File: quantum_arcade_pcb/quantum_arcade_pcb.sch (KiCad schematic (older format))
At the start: 429 parts, among them J20 J20, Q10 2N3904, Q11 2N3904, Q15 2N6044, Q16 2N6044, Q17 2N3904, Q7 2N3904, Q8 2N3906, Q9 2N3904, SW1 SW_DIP_x08, SW2 SW_DIP_x08, Y1 12.096MHz

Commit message: Finished 13 of 14 schematic pages
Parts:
- added A_5: LS157A, symbol quantum_arcade_pcb:LS157A
- added B_5, C_5: LS157B, symbol quantum_arcade_pcb:LS157B
- added B_6: AVG, symbol Star_Wars_Vector_PCB:AVG
- added C63: 220pf, symbol Device:C
- added unit 6 of F/H_4
- added F_8: LS175, symbol quantum_arcade_pcb:LS175
- added H_5: LS174, symbol quantum_arcade_pcb:LS174
- added H_6: S129, symbol Star_Wars_Vector_PCB:S129
- added H_7: LS00, symbol Star_Wars_Vector_PCB:LS00
- added H_8: LS399, symbol quantum_arcade_pcb:LS399
- added unit 3 of J_10
- added unit 4 of J_4
- added unit 2 of J_4
- added J_6: LS42, symbol Star_Wars_Vector_PCB:LS42
- added J_7: LS175A, symbol quantum_arcade_pcb:LS175A
- added J_8: LS175B, symbol quantum_arcade_pcb:LS175B
- added J_9: LS260, symbol Star_Wars_Vector_PCB:S260
- added K_6: LS109, symbol Star_Wars_Vector_PCB:LS109
- added K_7: LS32, symbol Star_Wars_Vector_PCB:LS32
- added unit 2 of K_8
- added unit 3 of K_8
- added unit 1 of K_8
- added L_5, M_5, M_6, M_7: LS161, symbol Star_Wars_Vector_PCB:LS161
- added unit 6 of L_6
- added unit 5 of L_6
- added L_7: S260, symbol Star_Wars_Vector_PCB:S260
- added L_8: S02, symbol Star_Wars_Vector_PCB:LS02
- added unit 4 of N_6
- added N_7: LS164, symbol quantum_arcade_pcb:LS164
- added unit 4 of P_8
- added Q12: 2N3906, TO_SOT_Packages_THT:TO-92_Molded_Narrow, symbol Star_Wars_Vector_PCB-rescue:2N3906
- added Q13, Q14: 2N3904, TO_SOT_Packages_THT:TO-92_Molded_Narrow, symbol Star_Wars_Vector_PCB-rescue:2N3904
- added R140: 1.2k, symbol Device:R_US
- added R141: 2.2k, symbol Device:R_US
- added R142: 4.7k, symbol Device:R_US
- added R143: 10k, symbol Device:R_US
- added R144: 22k, symbol Device:R_US
- added R145: 3.3k, symbol Device:R_US
- added R146: 510, symbol Device:R_US
- added R147, R148: 1k, symbol Device:R_US
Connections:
- net +5V: now also A_5.16 (VCC), B_5.16 (VCC), B_6.37 (VDD), C_5.16 (VCC), F_8.16 (VCC), H_5.16 (VCC), H_6.16 (VCC), H_8.16 (VCC), J_6.16 (VCC), J_7.16 (VCC), J_8.16 (VCC), J_9.14 (VCC), K_6.16 (VCC), K_7.14 (VCC), K_8.14 (VCC), L_5.16 (VCC), L_7.14 (VCC), M_5.16 (VCC), M_6.16 (VCC), M_7.16 (VCC), N_7.14 (VCC), Q13.3 (C), R145.2, R146.2
- net 1.5M: now also K_6.13 (K), K_6.3 (K), L_8.8, P_8.9
- net 12M: now also K_6.12 (Cp), K_6.4 (Cp), L_5.2 (CLK), M_5.2 (CLK), M_6.2 (CLK), M_7.2 (CLK)
- net 3M: now also L_7.12, N_7.8 (CLK)
- net 6M: now also L_7.3
- net AB1: now also C_5.14 (4A)
- net AB10: now also A_5.2 (1A)
- net AB11: now also A_5.5 (2A)
- net AB12: now also A_5.11 (3A)
- net AB2: now also C_5.11 (3A)
- net AB3: now also C_5.5 (2A)
- net AB4: now also C_5.2 (1A)
- net AB5: now also B_5.14 (4A)
- net AB6: now also B_5.11 (3A)
- net AB7: now also B_5.5 (2A)
- net AB8: now also B_5.2 (1A)
- net AB9: now also A_5.14 (4A)
- net AM1: now also C_5.12 (4Y)
- net AM10: now also A_5.4 (1Y)
- net AM11: now also A_5.7 (2Y)
- net AM2: now also C_5.9 (3Y)
- net AM3: now also C_5.7 (2Y)
- net AM4: now also C_5.4 (1Y)
- net AM5: now also B_5.12 (4Y)
- net AM6: now also B_5.9 (3Y)
- net AM7: now also B_5.7 (2Y)
- net AM8: now also B_5.4 (1Y)
- net AM9: now also A_5.12 (4Y)
- net DVG12: now also J_7.4 (D0), J_8.5 (D1)
- net DVG13: now also J_7.12 (D2), J_8.12 (D2)
- net DVG14: now also J_7.13 (D3), J_8.13 (D3)
- net DVG15: now also J_7.5 (D1), J_8.4 (D0)
- net DVY0: now also B_6.32 (DVY0)
- net DVY1: now also B_6.31 (DVY1)
- net DVY10: now also B_6.29 (DVY10)
- net DVY11: now also B_6.28 (DVY11)
- net DVY2: now also B_6.30 (DVY2)
- net DVY3: now also B_6.7 (DVY3)
- net DVY4: now also B_6.8 (DVY4), F_8.13 (D3)
- net DVY5: now also B_6.9 (DVY5), F_8.12 (D2)
- net DVY6: now also B_6.10 (DVY6), F_8.5 (D1)
- net DVY7: now also B_6.11 (DVY7), F_8.4 (D0)
- net DVY8: now also B_6.12 (DVY8)
- net DVY9: now also B_6.13 (DVY9)
- net GND: now also A_5.15 (E), A_5.8 (GND), B_5.15 (E), B_5.8 (GND), B_6.14 (GND), B_6.27 (DVY12), C_5.15 (E), C_5.8 (GND), F_8.8 (GND), H_5.8 (GND), H_6.13 (CE1), H_6.14 (CE2), H_6.8 (GND), H_8.8 (GND), J_6.8 (GND), J_7.8 (GND), J_8.8 (GND), J_9.11, J_9.13, J_9.7 (GND), K_6.8 (GND), K_7.7 (GND), K_8.7 (GND), L_5.8 (GND), L_7.13, L_7.7 (GND), M_5.8 (GND), M_6.8 (GND), M_7.8 (GND), N_7.7 (GND), Q12.1 (E), Q14.1 (E), R144.1, R147.1
- net PR219: now also L_5.1 (C), M_5.1 (C)
- net PR221: now also K_6.1 (Cd), K_6.11 (Sd), K_6.5 (Sd), M_6.1 (C), M_7.1 (C), M_7.4 (B), M_7.5 (C), M_7.6 (D), N_7.9 (C)
- net PR222: now also J_7.1 (C)
- net SCALELO: now also K_7.11
- net VCTR: now also H_8.9 (CLK), K_7.5, N_7.1 (A), N_7.2 (B)
- net ZREF: now also Q13.1 (E), R147.2
- net ~DISRST: now also F_8.1 (C), H_5.1 (C)
- net ~DVY11: now also K_8.10
- net ~LATCH1: now also H_7.10, J_6.2 (1), J_7.9 (CK), J_8.1 (C), L_6.11
- net ~STATCLK: now also K_8.6, K_8.9
- net ~V68K: now also A_5.1 (S), B_5.1 (S), C_5.1 (S)
- net ~VGGO: now also B_6.6 (~VGGO)
- net at B_8.10 (S1): now also A_8.10 (S1), C_8.10 (S1), H_7.11
- net at B_8.9 (S0): now also A_8.9 (S0), C_8.9 (S0), L_6.12
- net at B_7.10 (S1): now also A_7.10 (S1), C_7.10 (S1), H_7.8
- net at B_7.9 (S0): now also A_7.9 (S0), C_7.9 (S0), L_6.10
- new net: J_10.5, M_7.15 (RCO)
- new net: K_7.12, K_7.3, K_8.5
- new net: B_6.1 (AVG3), C_5.6 (2B)
- new net: B_5.10 (3B), B_6.15 (AVG6)
- new net: B_5.6 (2B), B_6.16 (AVG7)
- new net: B_5.3 (1B), B_6.17 (AVG8)
- new net: A_5.13 (4B), B_6.18 (AVG9)
- new net: A_5.3 (1B), B_6.19 (AVG10)
- new net: B_6.2 (AVG4), C_5.3 (1B)
- new net: A_5.6 (2B), B_6.20 (AVG11)
- new net: A_5.10 (3B), B_6.21 (AVG12)
- new net: B_5.13 (4B), B_6.3 (AVG5)
- new net: B_6.39 (AVG1), C_5.13 (4B)
- new net: B_6.40 (AVG2), C_5.10 (3B)
- new net: H_5.4 (2D), H_6.12 (O1), J_6.15 (A0)
- new net: H_6.15 (A7), J_4.13
- new net: H_5.15 (6Q), H_6.4 (A3)
- new net: H_5.5 (2Q), H_6.5 (A0)
- new net: H_5.12 (5Q), H_6.6 (A1)
- new net: H_5.2 (1Q), H_6.7 (A2)
- new net: H_5.14 (6D), H_6.9 (O4), K_6.15 (Cd)
- new net: H_5.7 (3Q), J_4.12
- new net: H_5.9 (CK), K_6.7 (~Q)
- new net: K_6.14 (J), K_6.2 (J), L_7.5
- new net: L_7.1, L_8.10
- new net: L_7.2, P_8.8
- new net: H_8.1 (WS), J_9.6
- new net: H_8.10 (QC), J_9.3, R142.2
- new net: H_8.15 (QD), J_9.12, R143.2
- new net: H_8.2 (QA), J_9.1, R140.2
- new net: F_8.7 (Q1), H_8.3 (A1)
- new net: F_8.2 (Q0), H_8.4 (A2)
- new net: F_8.10 (Q2), H_8.5 (B2)
- new net: F_8.15 (Q3), H_8.6 (B1)
- new net: H_8.7 (QB), J_9.2, R141.2
- new net: N_6.12, N_7.10 (QE)
- new net: N_6.11, N_7.11 (QF)
- new net: J_9.5, K_8.1
- new net: Q12.2 (B), Q14.3 (C), R140.1, R141.1, R142.1, R143.1, R144.2, R145.1
- new net: K_8.2, N_6.13
- new net: F_8.9 (CK), K_8.8
- new net: C63.2, K_8.3, R148.2
- new net: C63.1, Q14.2 (B), R148.1
- new net: Q12.3 (C), Q13.2 (B), R146.1
- new net: L_5.15 (RCO), M_5.10 (ET), M_5.7 (EP), M_6.7 (EP), M_7.7 (EP)
- new net: M_5.11 (QD), M_5.5 (C)
- new net: M_5.12 (QC), M_5.4 (B)
- new net: M_5.13 (QB), M_5.3 (A)
- new net: L_5.6 (D), M_5.14 (QA)
- new net: M_5.15 (RCO), M_6.10 (ET)
- new net: M_5.6 (D), M_6.14 (QA)
- new net: J_4.4, L_5.9 (LD), M_5.9 (LD), M_6.9 (LD), M_7.9 (LD)
- new net: M_6.11 (QD), M_6.5 (C)
- new net: M_6.12 (QC), M_6.4 (B)
- new net: M_6.13 (QB), M_6.3 (A)
- new net: M_6.15 (RCO), M_7.10 (ET)
- new net: M_6.6 (D), M_7.14 (QA)
- new net: M_7.13 (QB), M_7.3 (A)
- new net: L_5.11 (QD), L_5.5 (C)
- new net: L_5.12 (QC), L_5.4 (B)
- new net: L_5.13 (QB), L_5.3 (A)
- new net CNTR: K_7.4
- new net DVY12: J_7.2 (Q0), K_8.4
- new net GO: J_4.11, K_7.6, L_5.10 (ET), L_5.7 (EP)
- new net NORM: J_4.5
- new net OP0: H_6.3 (A4), J_7.10 (Q2)
- new net OP1: H_6.2 (A5), J_7.15 (Q3)
- new net OP2: H_6.1 (A6), J_7.7 (Q1), K_7.1
- new net OPO1: B_6.33 (OP1)
- new net SCALE: J_4.6
- new net ST1: H_5.13 (5D), H_6.11 (O2), J_6.14 (A1)
- new net ST2: B_6.35 (ST2), H_5.3 (1D), H_6.10 (O3), J_6.13 (A2)
- new net ST3: B_6.38 (ST3), J_6.12 (A3), K_6.9 (~Q)
- new net STROBE2: K_7.2
- new net VHALT: H_5.6 (3D)
- new net Z0: J_8.7 (Q1), J_9.10
- new net Z1: J_8.10 (Q2), J_9.9
- new net Z2: J_8.15 (Q3), J_9.8
- new net Z3: J_8.2 (Q0), J_9.4
- new net ~68K: L_8.9
- new net ~DVY12: J_7.3 (~Q0), K_7.13
- new net ~ENORM: H_7.12, H_7.9
- new net ~LATCH3: H_7.13, J_6.4 (3), J_8.9 (CK), L_6.13
- new net ~OP0: J_7.11 (~Q2)
- new net ~OP2: J_7.6 (~Q1)
- new net ~OPO0: B_6.26 (~OP0)
- new net ~OPO2: B_6.5 (~OP2)
- new net ~STOP: J_10.6
- new net ~STROBE0: B_6.24 (~STROBE0), J_6.5 (4)
- new net ~STROBE1: B_6.34 (~STROBE1), J_6.6 (5)
- new net ~STROBE2: B_6.4 (~STROBE2), J_6.7 (6)
- new net ~STROBE3: J_6.9 (7)
- new net ~VRAM0: A_5.9 (3Y), F/H_4.13
- new net ~VRAM1: F/H_4.12
- new net ~Z1: J_8.11 (~Q2)
- no-connect marks 46 -> 77
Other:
- note added: "INTENSITY CORRECTION"
- note added: "OPCODE AND INTENSITY LATCHES"
- note added: "STATE MACHINE"
- note added: "VECTOR ADDRESS CONTROLLER"
- note added: "VECTOR DATA SHIFTERS"
- note added: "VECTOR TIMER"
- note added: "Z INTENSITY"
- moved on the sheet: A_3A, A_3B, A_3C, A_3E, A_7, A_8, B_1, B_2/3, B_7, B_8, C71, C72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

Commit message: Finished initial schematic
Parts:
- added F_6: LS00, symbol Star_Wars_Vector_PCB:LS00
- added unit 1 of J_4
- added J_5: S74, symbol Star_Wars_Vector_PCB:LS74
- added K_10: S86, symbol Star_Wars_Vector_PCB:LS86
- added unit 4 of K_4
- added unit 3 of K_4
- added K_5: LS27, symbol Star_Wars_Vector_PCB:LS27
- added unit 3 of K_7
- added K_9: LS109, symbol Star_Wars_Vector_PCB:LS109
- added unit 2 of L_7
- added unit 2 of L_8
- added unit 4 of L_8
- added L_9: LS175, symbol quantum_arcade_pcb:LS175
- added M_8: LS191A, symbol Star_Wars_Vector_PCB:LS191A
- added unit 6 of P_8
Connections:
- net +5V: now also J_4.14 (VCC), J_5.14 (VCC), K_9.16 (VCC), L_9.16 (VCC), M_8.16 (VCC)
- net 1.5M: now also K_7.9
- net 12M: now also K_9.12 (Cp), K_9.4 (Cp)
- net CNTR: now also K_9.6 (Q), L_7.10
- net DVX10: now also K_10.9
- net DVX11: now also K_10.10
- net DVY10: now also K_10.5, L_9.4 (D0), L_9.5 (D1)
- net DVY11: now also K_10.4
- net DVY8: now also L_9.13 (D3)
- net DVY9: now also L_9.12 (D2)
- net GND: now also J_4.7 (GND), J_5.7 (GND), K_9.8 (GND), L_9.8 (GND), M_8.8 (GND), M_8.9 (D)
- net NORM: now also F_6.5, J_5.9 (2Q)
- net OP0: now also J_5.12 (2D), J_5.2 (1D), K_5.10
- net OP2: now also K_5.11, L_8.11
- net PR221: now also J_5.10 (~1PRE_), K_9.11 (Sd), K_9.5 (Sd), M_8.5 (D/U)
- net SCALE: now also L_7.4, L_8.4
- net SCALELO: now also L_9.9 (CK)
- net VCTR: now also K_9.10 (Q), L_7.11
- net VHALT: now also J_5.5 (1Q)
- net ~CENTER: now also K_4.11
- net ~DISRST: now also J_5.4 (~1PRE_), K_4.8, L_9.1 (C)
- net ~OP2: now also J_4.2
- net ~RESET: now also K_4.10
- net ~STOP: now also K_9.13 (K), K_9.3 (K)
- net ~STROBE0: now also J_5.11 (2CLK)
- net ~STROBE1: now also L_8.12
- net ~STROBE3: now also J_5.3 (1CLK), K_7.10
- net ~VCTR: now also K_9.9 (~Q)
- net ~VGGO: now also J_5.1 (~1CLR)
- net ~VGRST: now also K_4.9
- net ~WEL: now also N_4.8
- net ~COLORAMWR: now reaches F_5.3
- new net: J_5.6 (~1Q), K_4.12, K_9.1 (Cd), K_9.15 (Cd)
- new net: J_4.1, K_9.2 (J)
- new net: K_4.13, K_9.7 (~Q)
- new net: K_5.8, K_9.14 (J)
- new net: J_4.3, K_5.9, K_7.8
- new net: F_6.4, J_5.13 (~1CLR), L_7.6
- new net: K_10.6, L_7.8
- new net: K_10.8, L_7.9
- new net: L_9.10 (Q2), M_8.1 (B)
- new net: L_9.15 (Q3), M_8.15 (A)
- new net: L_9.7 (Q1), M_8.10 (C)
- new net: M_8.11 (LD), P_8.12
- new net: L_8.6, M_8.12 (M/M), M_8.4 (G)
- new net: L_8.13, L_8.5, P_8.13
- new net ENORM: F_6.6
- new net ~12M: M_8.14 (CK)
- no-connect marks 77 -> 88
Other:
- note added: "CENTER FLAG"
- note added: "NORMALIZATION FLAG"
- note added: "VECTOR FLAG"
- note added: "VECTOR HALT FLAG"
- note added: "VECTOR SCALING"

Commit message: Fixed all schematic errors
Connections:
- net DISRST is gone; now on net ~DISRST: D_8.1 (C)
- net ENORM is gone; now on net ~ENORM: F_6.6
- net OPO1 is gone; now on net OP1: B_6.33 (OP1)
- net POR is gone; now on net ~POR: P_4.13
- net R\~WB is gone; now on net ~WEL: N_4.5
- net STROBE2 is gone; now on net ~STROBE2: K_7.2
- net VRAM0 is gone; now on net ~VRAM0: D_5.18 (~CE), E_5.18 (~CE)
- net VRAM1 is gone; now on net ~VRAM1: D_6.18 (~CE), E_6.18 (~CE)
- net ~12M is gone; now on net 12M: M_8.14 (CK)
- net ~68K is gone; now on net ~V68K: L_8.9
- net ~COLORAMWR is gone; now on net ~COLORAMWA: F_5.3
- net ~MTDACK is gone; now on net ~MDTACK: P_4.10, R_2.12 (2D), R_2.5 (1Q)
- net ~OPO0 is gone; now on net ~OP0: B_6.26 (~OP0)
- net ~OPO2 is gone; now on net ~OP2: B_6.5 (~OP2)
- net ~VHALT is gone; now on net VHALT: M_9.6 (I2a)
- net A14: no longer D_1.1 (A)
- net AB14: now also D_1.1 (A)
- net Z0: now also H_8.14 (D1)
- net Z1: now also H_8.11 (C1); no longer J_9.9
- net ~DTACK: no longer P_4.9
- net ~DTACK2: now also P_4.9
- net ~Z1: now also J_9.9
- net ST1: no longer names the net of H_5.13 (5D), H_6.11 (O2), J_6.14 (A1)
- net ~MDTACL renamed ~MDTACK
- net ~RESET*: no longer names the net of K_4.2, L_4.6 (~1Q)

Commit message: Placed all ICs on the PCB
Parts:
- added C_9, E_9: Spare16, Star_Wars_Vector_PCB:DIP16, symbol quantum_arcade_pcb:Spare16
- added unit 1 of F_6
- added unit 1 of H_7
- added unit 1 of K_10
- added unit 1 of K_5
- added unit 1 of L_6
- added unit 1 of L_8
- added unit 1 of N_6
- added unit 1 of P_6
- A_3, B_11, B_12, C_11, C_12, C_3, F/H_4, F_5, F_6, H_7, J_10, J_4, J_5, J_9, K_10, K_4, K_5, K_7, K_8, L_4, L_6, L_7, L_8, M_4, N_10, N_4, N_6, N_7, P_11, P_4, P_5, P_6, P_8, R_10, R_2, R_4: footprint (none) -> Star_Wars_Vector_PCB:DIP14
- A_5, A_7, A_8, B_5, B_7, B_8, C_5, C_7, C_8, D_1, D_7, E_7, F_7, F_8, H/J_4, H_5, H_6, H_8, J_6, J_7, J_8, K_6, K_9, L_5, L_9, M_5, M_6, M_7, M_8, N_8, P_10, P_7, P_9, R_6, SW1, SW2: footprint (none) -> Star_Wars_Vector_PCB:DIP16
- B_1, D/E_4, D_8, E/F_4, E_1, F_1, M_9, N_1, N_5, N_9, P_1, P_2, P_3: footprint (none) -> Star_Wars_Vector_PCB:DIP20
- B_2/3, B_6, D_2/3: footprint (none) -> Star_Wars_Vector_PCB:DDIP40
- C10, C11, C12, C13, C14, C15, C16, C17, C18, C19, C2, C20, C26, C27, C28, C29, C3, C30, C31, C32, C33, C34, C35, C36, C39, C40, C41, C9, CR1, R106, R180, R181, R182, R183, R184, R185, R186, R187, R26, R27, R30, R31, R32, R33, R34, R35, R36, R37, R38, R39, R40, R41, R44, R45, R46, R48, R49, R50, R51, R52, R53, R54, R55, R58, R59, R60, R61, R62, R63, R64, R65, R66, R67, R69, R70, R71, R73, R75, R76, R77, R78, R79, R80, R81, R82, R83, R84, R85, R86, R87, R89, R90, R91, R93, R94, R95, R96, R97, RV1, RV2: footprint Star_Wars_Vector_PCB:GenericComp -> (none)
- C21, C4: footprint Star_Wars_Vector_PCB:SmallCap -> (none)
- C25, C8: footprint Star_Wars_Vector_PCB:CapYellow -> (none)
- C37, C38, C42: footprint Star_Wars_Vector_PCB:CapBrown -> (none)
- C83, C84, C85, C86, C87, C88, C89, C90, R110, R111, R112, R113, R114, R115, R116, R117: footprint (none) -> quantum_arcade_pcb:GenComp
- D_5, D_6, E_5, E_6, M_2, M_3, N_2, N_3: footprint (none) -> Star_Wars_Vector_PCB:DDIP24
- E_2, E_3, F_2, F_3, H/J_2, H/J_3, K_2, K_3, L_2, L_3: footprint (none) -> Star_Wars_Main_PCB:DIP28
- J20: footprint (none) -> Asteroids:J20
- K/L_1: footprint (none) -> quantum_arcade_pcb:DIP64
- M/N_12: footprint (none) -> Star_Wars_Vector_PCB:DIP8
- Q10, Q11, Q12, Q13, Q14, Q9: footprint TO_SOT_Packages_THT:TO-92_Molded_Narrow -> (none)
- Q17: footprint Package_TO_SOT_THT:TO-92_Inline -> (none)
- Q7, Q8: footprint Star_Wars_Vector_PCB:GenericTrans -> (none)
- R42, R43, R47, R68, R72, R74, R88, R92: footprint Star_Wars_Vector_PCB:PotBlk -> (none)
- R_3: footprint (none) -> Star_Wars_Vector_PCB:DIP18
- R_5: renamed from UR_5; footprint (none) -> Star_Wars_Vector_PCB:DIP14
- TPXOUT1, TPYOUT1: footprint Star_Wars_Vector_PCB:TEST_POINT -> (none)
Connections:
- net +5V: now also F_6.14 (VCC), H_7.14 (VCC), K_10.14 (VCC), K_5.14 (VCC), L_6.14 (VCC), L_8.14 (VCC), N_6.14 (VCC), P_6.14 (VCC)
- net GND: now also F_6.7 (GND), H_7.7 (GND), K_10.7 (GND), K_5.7 (GND), L_6.7 (GND), L_8.7 (GND), N_6.7 (GND), P_6.7 (GND)
- no-connect marks 88 -> 144

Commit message: Placed several components
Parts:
- added C130: .047uf, quantum_arcade_pcb:GenComp, symbol Device:C
- C100, C101, C102, C103, C104, C105, C106, C129, C63, C64, C65, C67, C68, C69, C70, C78, C79, C80, C81, C91, C92, C93, C94, C95, C96, C98, C99, R118, R119, R120, R121, R122, R123, R124, R125, R126, R127, R128, R129, R130, R131, R132, R133, R134, R135, R136, R137, R138, R139, R140, R141, R142, R143, R144, R145, R146, R147, R148, R149, R151, R152, R153, R155, R156, R157, R158, R159, R160, R161, R162, R171, R172, R188, R189, R190, R191, R192, R193, R194, R195, R196, R197, R198, R199, R200, R201, R202, R203, R204, R205, R206, R207, R208, R209, R210, R211, R212, R213, R216, R217, R218, R221: footprint (none) -> quantum_arcade_pcb:GenComp
- L1, L2, L3, L4: footprint (none) -> quantum_arcade_pcb:Ind
- Q10, Q11, Q12, Q13, Q14, Q9: footprint (none) -> quantum_arcade_pcb:GenTrans
- TPAUD1, TPAUD2, TPGND1: footprint (none) -> quantum_arcade_pcb:TP
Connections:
- net BLUE: now also R225.2; no longer L3.2
- net GND: now also Q12.3 (C); no longer Q12.1 (E)
- net GREEN: now also R226.2; no longer L4.2
- net RED: now also R224.2; no longer L2.2
- net at A_3.6 (-), B_2/3.37 (AUD), R205.2: now also C130.1
- net at A_3.7, C79.1, R205.1: now also C130.2
- net at Q9.1 (E), R137.1: now also L2.1; no longer R224.1
- net at Q10.1 (E), R138.1: now also L3.1; no longer R225.1
- net at Q11.1 (E), R139.1: now also L4.1; no longer R226.1
- net at Q13.2 (B), R146.1: now also Q12.1 (E); no longer Q12.3 (C)
- new net: L4.2, R226.1
- new net: L3.2, R225.1
- new net: L2.2, R224.1
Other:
- moved on the sheet: L2, L3, L4, R224, R225, R226

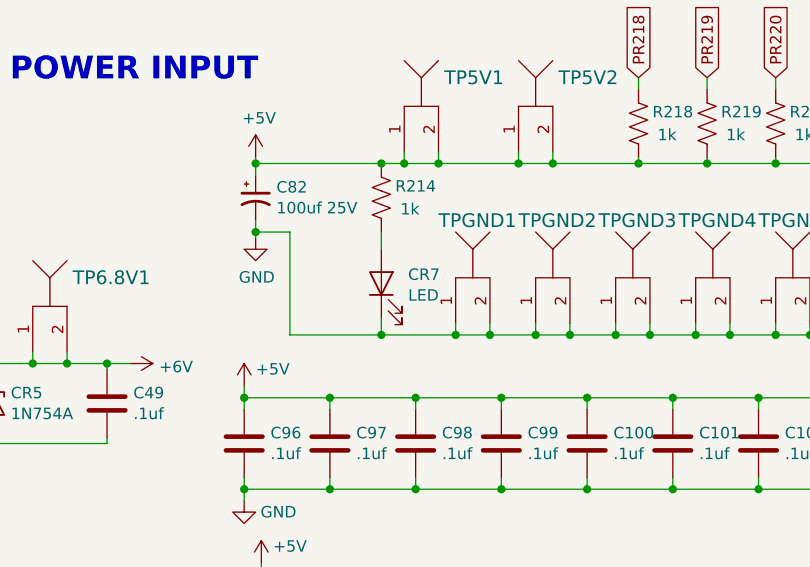
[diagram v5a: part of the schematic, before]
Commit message: 133 components left to place
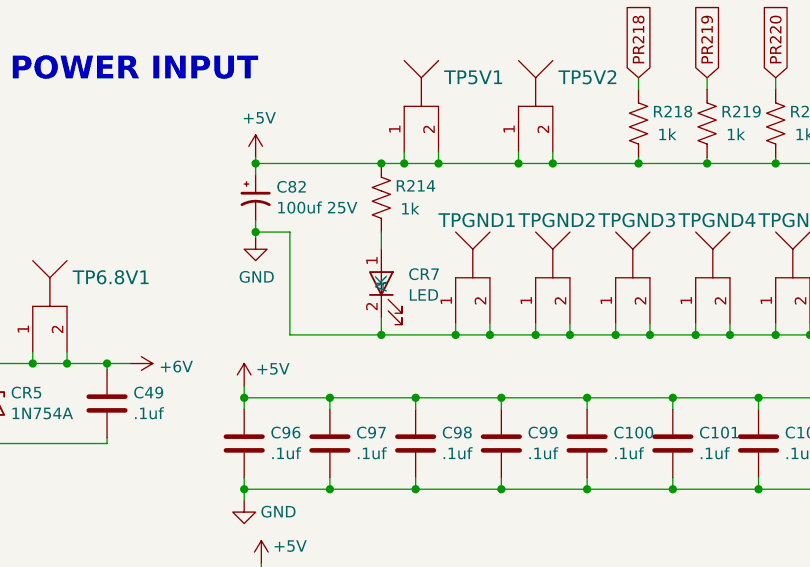
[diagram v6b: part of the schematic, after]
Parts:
- removed CR7: LED, symbol Device:LED
- added CR7: LED, quantum_arcade_pcb:LED, symbol quantum_arcade_pcb:LED
- C107, C108, C109, C110, C111, C112, C113, C114, C115, C116, C117, C118, C119, C120, C121, C122, C123, C124, C125, C126, C127, C128, C51, C61, C71, C72, C73, C75, C97, R163, R164, R165, R166, R167, R168, R169, R170, R173, R174, R175, R176, R177, R178, R179, R180, R181, R182, R183, R184, R185, R186, R187, R214, R215, R219, R220, R222, R223, R224, R225, R226: footprint (none) -> quantum_arcade_pcb:GenComp
- C44, C46, C82: footprint (none) -> quantum_arcade_pcb:Cap2
- C45, C48, C52, C53, C54, C55, C56, C57, C58, C59, C60, C62, C74: footprint (none) -> quantum_arcade_pcb:Cap1
- C47: footprint (none) -> quantum_arcade_pcb:Cap3
- C76, C77: footprint (none) -> quantum_arcade_pcb:CapSmall
- CR6: footprint (none) -> quantum_arcade_pcb:Diode
- Q15, Q16, VR1, VR2: footprint (none) -> quantum_arcade_pcb:BigTrans
- Q17: footprint (none) -> quantum_arcade_pcb:GenTrans
- TP12M1, TPBLU1, TPGRN1, TPRED1, TPRESET1, TPRESET2, TPWDDIS1: footprint (none) -> quantum_arcade_pcb:TP
- Y1: footprint (none) -> quantum_arcade_pcb:Crystal
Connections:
- net GND: now also CR7.2 (K)
- net at R214.1: now also CR7.1 (A)

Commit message: 80 components left to place
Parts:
- C11, C15, C16, C28, C33, C34, R34, R35, R36, R37, R38, R40, R44, R45, R50, R51, R52, R53, R60, R61, R63, R64, R65, R67, R69, R70, R77, R78, R79, R80, R87, R89, R91, R93: footprint (none) -> quantum_arcade_pcb:GenComp
- C42: footprint (none) -> quantum_arcade_pcb:CapSmall
- R42, R43, R47, R68, R72, R74, R88, R92: footprint (none) -> Star_Wars_Vector_PCB:PotBlk
- TP5V1, TPGND2: footprint (none) -> quantum_arcade_pcb:TP
